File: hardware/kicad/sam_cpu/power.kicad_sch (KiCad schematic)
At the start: 51 parts, among them J11 J11 POWER, J17 EXT 5V, J23 EXT 12V, Q19 DMP3013SFV, Q20 DMP3013SFV, U1 TPS2117, U3 NCP1117-3.3, U33 LTC4412, U34 LTC4412, U35 TPS54302

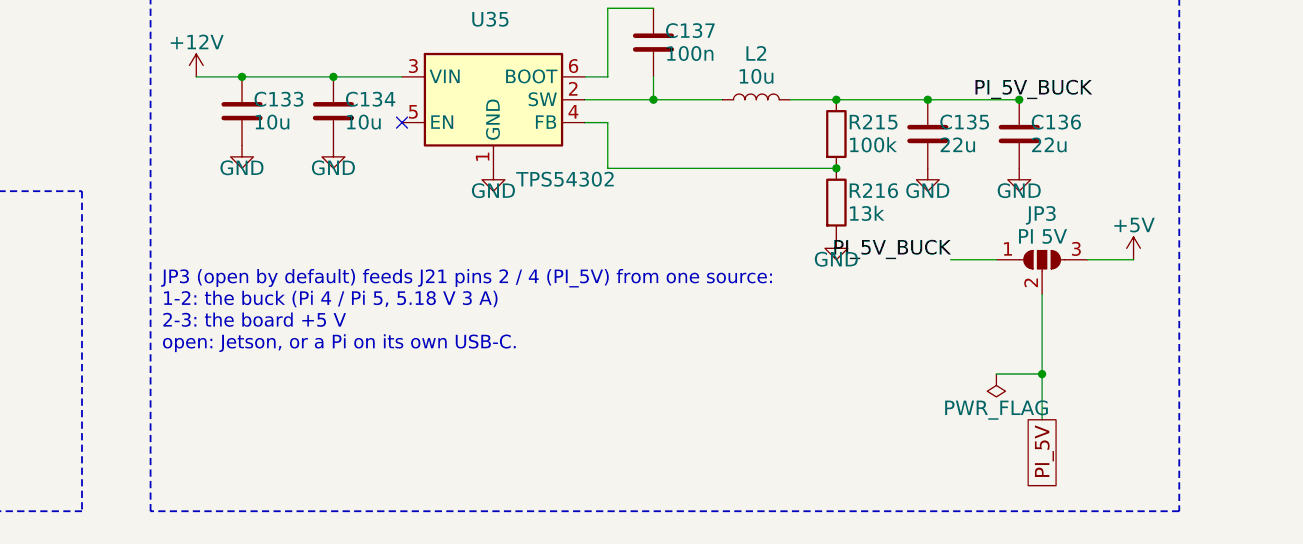
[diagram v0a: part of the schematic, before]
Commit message: Pi header 5 V: JP3 becomes a 3-pin header with one jumper shunt
One shunt can only sit on one pair, so the board +5 V and the buck can never both
feed J21. The header is a right-angle 1x3 2.54 mm (PZ254R-11-03P, LCSC C492411,
shunt C100114), about 2.5 mm high, so it stays under the Pi below the buck, pads on
y 159.5: pin 1 +5V, pin 2 PI_5V, pin 3 PI_5V_BUCK (1-2 board, 2-3 buck, no shunt
for a Jetson). c46 (schematic) and c47 (board); 23 unconnected as before, no new
DRC errors, schematic parity unchanged.

Co-Authored-By: Claude Opus 5.5 <noreply@anthropic.com>
Claude-Session: https://claude.ai/code/session_01QQate2kninVTv93dgZ4pfZ
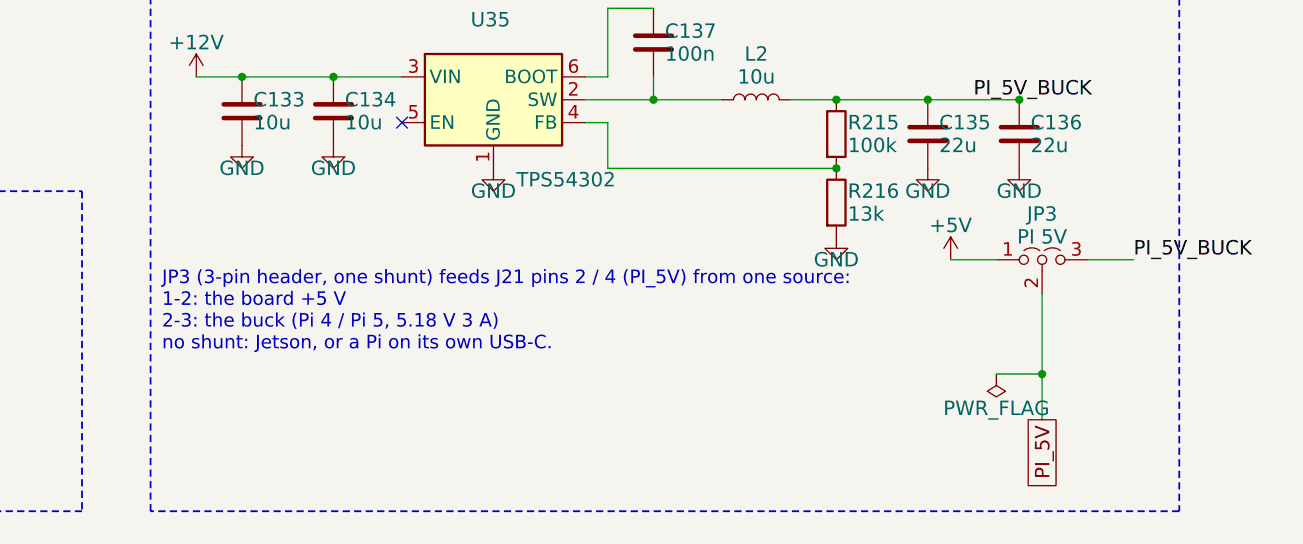
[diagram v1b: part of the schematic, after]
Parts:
- JP3: footprint Jumper:SolderJumper-3_P1.3mm_Open_RoundedPad1.0x1.5mm -> Connector_PinHeader_2.54mm:PinHeader_1x03_P2.54mm_Horizontal; symbol Jumper:SolderJumper_3_Open -> Jumper:Jumper_3_Open
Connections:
- net +5V: now also JP3.1 (A); no longer JP3.3 (B)
- net PI_5V_BUCK: now also JP3.3 (B); no longer JP3.1 (A)
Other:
- note added: "JP3 (3-pin header, one shunt) feeds J21 pins 2 / 4 (PI_5V) from one source: 1-2: the board +5 V 2-3: the buck (Pi 4 / Pi 5, 5.18 V 3 A) no shunt: Jetson, or a Pi on its own USB-C."
- note removed: "JP3 (open by default) feeds J21 pins 2 / 4 (PI_5V) from one source: 1-2: the buck (Pi 4 / Pi 5, 5.18 V 3 A) 2-3: the board +5 V open: Jetson, or a Pi on its own USB-C."
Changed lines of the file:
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@@
 		)
 	)
-	(text "JP3 (open by default) feeds J21 pins 2 / 4 (PI_5V) from one source:\n1-2: the buck (Pi 4 / Pi 5, 5.18 V 3 A)\n2-3: the board +5 V\nopen: Jetson, or a Pi on its own USB-C."
+	(text "JP3 (3-pin header, one shunt) feeds J21 pins 2 / 4 (PI_5V) from one source:\n1-2: the board +5 V\n2-3: the buck (Pi 4 / Pi 5, 5.18 V 3 A)\nno shunt: Jetson, or a Pi on its own USB-C."
 		(exclude_from_sim no)
 		(at 293.37 222.25 0)
@@
 	)
 	(symbol
-		(lib_id "Jumper:SolderJumper_3_Open")
+		(lib_id "Jumper:Jumper_3_Open")
 		(at 391.16 220.98 0)
 		(unit 1)
@@
 			)
 		)
-		(property "Footprint" "Jumper:SolderJumper-3_P1.3mm_Open_RoundedPad1.0x1.5mm"
+		(property "Footprint" "Connector_PinHeader_2.54mm:PinHeader_1x03_P2.54mm_Horizontal"
 			(at 391.16 220.98 0)
 			(hide yes)
@@
 			)
 		)
-		(property "Description" "Pi header 5 V: bridge 1-2 for the buck, 2-3 for the board +5 V, none for a Jetson (open by default)"
+		(property "Description" "Pi header 5 V jumper, right-angle 1x3 2.54 mm PZ254R-11-03P (LCSC C492411) + shunt C100114: 1-2 board +5 V, 2-3 buck, no shunt for a Jetson"
 			(at 391.16 220.98 0)
 			(hide yes)
@@
 		)
 	)
-	(label "PI_5V_BUCK"
-		(at 381 220.98 180)
-		(effects
-			(font
-				(size 1.6 1.6)
-			)
-			(justify right bottom)
-		)
-	)
 	(wire
 		(pts
@@
 			(width 0)
 			(type default)
-		)
-	)
-	(symbol
-		(lib_id "power:+5V")
-		(at 401.32 220.98 0)
-		(unit 1)
-		(body_style 1)
-		(exclude_from_sim no)
-		(in_bom no)
-		(on_board no)
-		(in_pos_files yes)
-		(dnp no)
-		(property "Reference" "#PWR01121"
-			(at 401.32 220.98 0)
-			(hide yes)
-			(show_name no)
-			(do_not_autoplace no)
-			(effects
-				(font
-					(size 1.6 1.6)
-				)
-			)
-		)
-		(property "Value" "+5V"
-			(at 401.32 217.17 0)
-			(show_name no)
-			(do_not_autoplace no)
-			(effects
-				(font
-					(size 1.6 1.6)
-				)
-			)
-		)
-		(property "Footprint" ""
-			(at 401.32 220.98 0)
-			(hide yes)
-			(show_name no)
-			(do_not_autoplace no)
-			(effects
-				(font
-					(size 1.6 1.6)
-				)
-			)
-		)
-		(property "Datasheet" ""
-			(at 401.32 220.98 0)
-			(hide yes)
-			(show_name no)
-			(do_not_autoplace no)
-			(effects
-				(font
-					(size 1.6 1.6)
-				)
-			)
-		)
-		(property "Description" "Power symbol creates a global label with name \"+5V\""
-			(at 401.32 220.98 0)
-			(hide yes)
-			(show_name no)
-			(do_not_autoplace no)
-			(effects
-				(font
-					(size 1.6 1.6)
-				)
-			)
-		)
-		(pin "1"
-		)
-		(instances
-			(project "sam_cpu"
-				(path "/2aea4fdf-a573-57d0-a5af-7bd6ce737647/febff99c-25e7-5ff2-ad94-91f07160e16c"
-					(reference "#PWR01121")
-					(unit 1)
-				)
-			)
 		)
 	)
@@
 		)
 	)
+	(symbol
+		(lib_id "power:+5V")
+		(at 381 220.98 0)
+		(unit 1)
+		(body_style 1)
+		(exclude_from_sim no)
+		(in_bom no)
+		(on_board no)
+		(in_pos_files yes)
+		(dnp no)
+		(property "Reference" "#PWR01131"
+			(at 381 220.98 0)
+			(hide yes)
+			(show_name no)
+			(do_not_autoplace no)
+			(effects
+				(font
+					(size 1.6 1.6)
+				)
+			)
+		)
+		(property "Value" "+5V"
+			(at 381 217.17 0)
+			(show_name no)
+			(do_not_autoplace no)
+			(effects
+				(font
+					(size 1.6 1.6)
+				)
+			)
+		)
+		(property "Footprint" ""
+			(at 381 220.98 0)
+			(hide yes)
+			(show_name no)
+			(do_not_autoplace no)
+			(effects
+				(font
+					(size 1.6 1.6)
+				)
+			)
+		)
+		(property "Datasheet" ""
+			(at 381 220.98 0)
+			(hide yes)
+			(show_name no)
+			(do_not_autoplace no)
+			(effects
+				(font
+					(size 1.6 1.6)
+				)
+			)
+		)
+		(property "Description" "Power symbol creates a global label with name \"+5V\""
+			(at 381 220.98 0)
+			(hide yes)
+			(show_name no)
+			(do_not_autoplace no)
+			(effects
+				(font
+					(size 1.6 1.6)
+				)
+			)
+		)
+		(pin "1"
+		)
+		(instances
+			(project "sam_cpu"
+				(path "/2aea4fdf-a573-57d0-a5af-7bd6ce737647/febff99c-25e7-5ff2-ad94-91f07160e16c"
+					(reference "#PWR01131")
+					(unit 1)
+				)
+			)
+		)
+	)
+	(label "PI_5V_BUCK"
+		(at 401.32 220.98 0)
+		(effects
+			(font
+				(size 1.6 1.6)
+			)
+			(justify left bottom)
+		)
+	)
